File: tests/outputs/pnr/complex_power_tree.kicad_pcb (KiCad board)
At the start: 6 copper layers, 50 x 50 mm, 30 parts

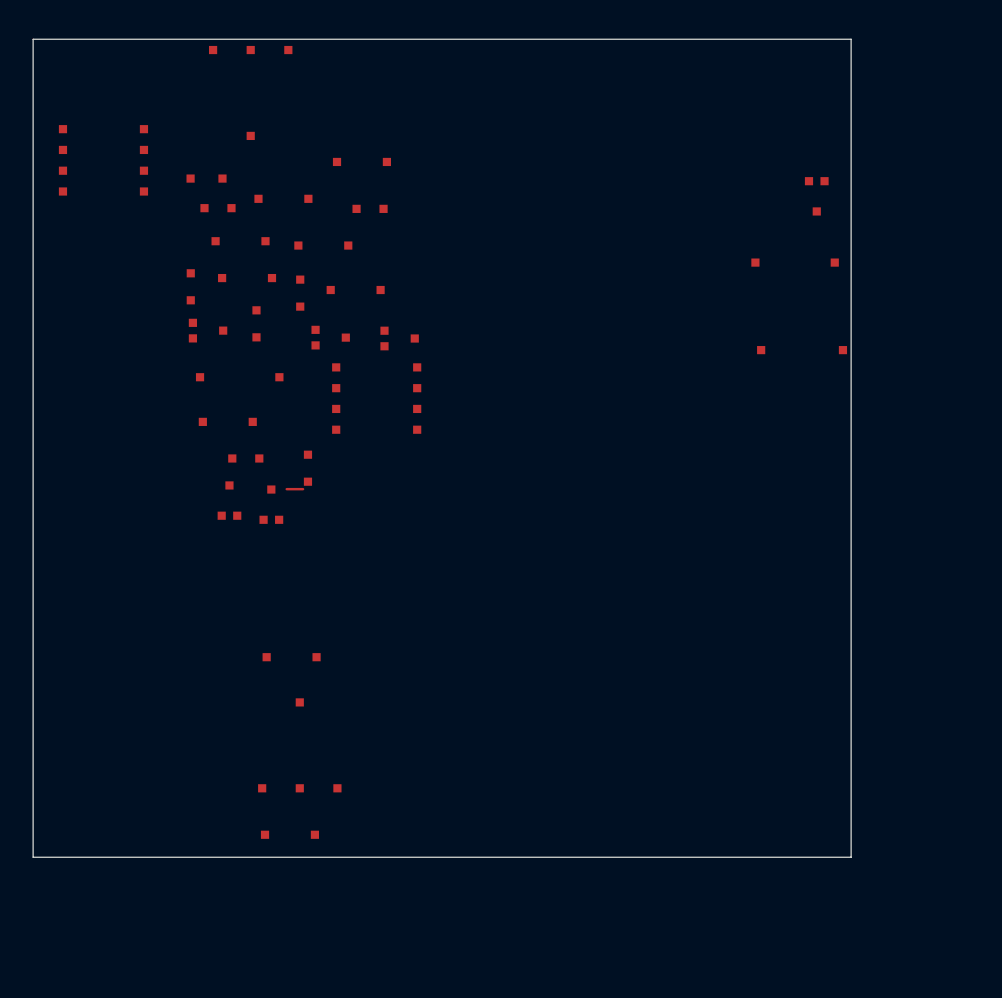
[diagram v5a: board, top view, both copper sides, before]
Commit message: feat: hierarchical block placement — zero overlaps
FPGA-inspired hierarchical placement:
1. Form blocks from functional groups + standalone components
2. Layout within blocks: IC center, caps flanking, inductors above,
   resistors below, diodes next to inductors
3. Place blocks on board using shelf packing (seed varies order)
4. Stamp block positions to individual components

Blocks guarantee zero overlaps since each block is pre-sized to
contain its children with internal routing margin.

Also: route through footprints — only block pad areas (not entire
component body), so traces can pass between pads.

Results on complex_power_tree.bhdl:
- Overlaps: 0 (was 2-19)
- 30/30 inside board
- Groups naturally clustered within blocks
- 16 blocks from 30 components (4 expansion + 12 singleton)
- Routability: 21% (routing channels now open between pads)

Co-Authored-By: Claude Opus 4.6 (1M context) <noreply@anthropic.com>
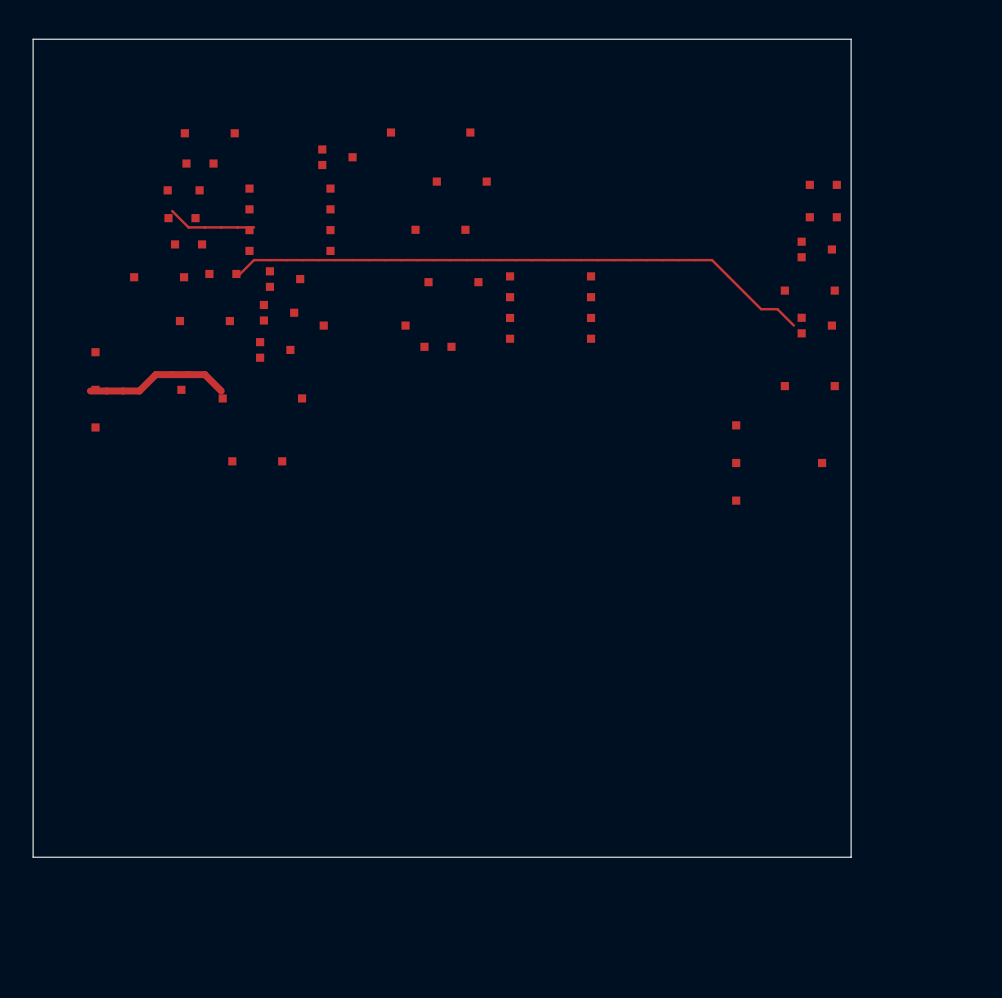
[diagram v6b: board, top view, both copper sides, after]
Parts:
- moved C5 42.0 mm to (47.5, 21.2)
- moved C4 38.8 mm to (47.5, 15.4), turned to 0 degrees
- moved R3 35.3 mm to (48.3, 10.9), turned to 0 degrees
- moved D4 35.1 mm to (47.9, 17.5), turned to 0 degrees
- moved U1 34.0 mm to (45.6, 25.9), turned to 360 degrees
- moved D2 33.6 mm to (15.0, 16.7), turned to 360 degrees
- moved R6 33.6 mm to (14.0, 22.0)
- moved R4 32.7 mm to (48.3, 8.90), turned to 360 degrees
- moved R2 26.8 mm to (20.3, 17.5)
- moved D3 26.1 mm to (47.9, 12.8)
- moved U2 19.4 mm to (6.44, 21.4), turned to 0 degrees
- moved C2 19.0 mm to (24.3, 5.70)
- moved R7 18.2 mm to (10.2, 7.60), turned to 360 degrees
- moved C9 13.7 mm to (10.5, 17.2), turned to 360 degrees
- moved R5 13.0 mm to (11.6, 14.3), turned to 0 degrees
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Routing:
- net 0: track 1.00 -> 50.3 mm

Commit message: feat: netlist-driven internal block layout
Replace template-based block layout with netlist-driven placement:
- For each child, find which IC pin it connects to via shared nets
- Place child on the side of IC where that pin is (left/right/top/bottom)
- Orient child so its connecting pin faces the IC
- Stack multiple children on the same side with spacing

Skip GND pins for side determination (GND connects everywhere).
Prefer signal/power pins that indicate actual signal flow direction.

3mm routing channels between blocks on the board.

Results: 6 overlaps (internal block stacking needs refinement),
29% routability with pad-only grid blockage.

Co-Authored-By: Claude Opus 4.6 (1M context) <noreply@anthropic.com>
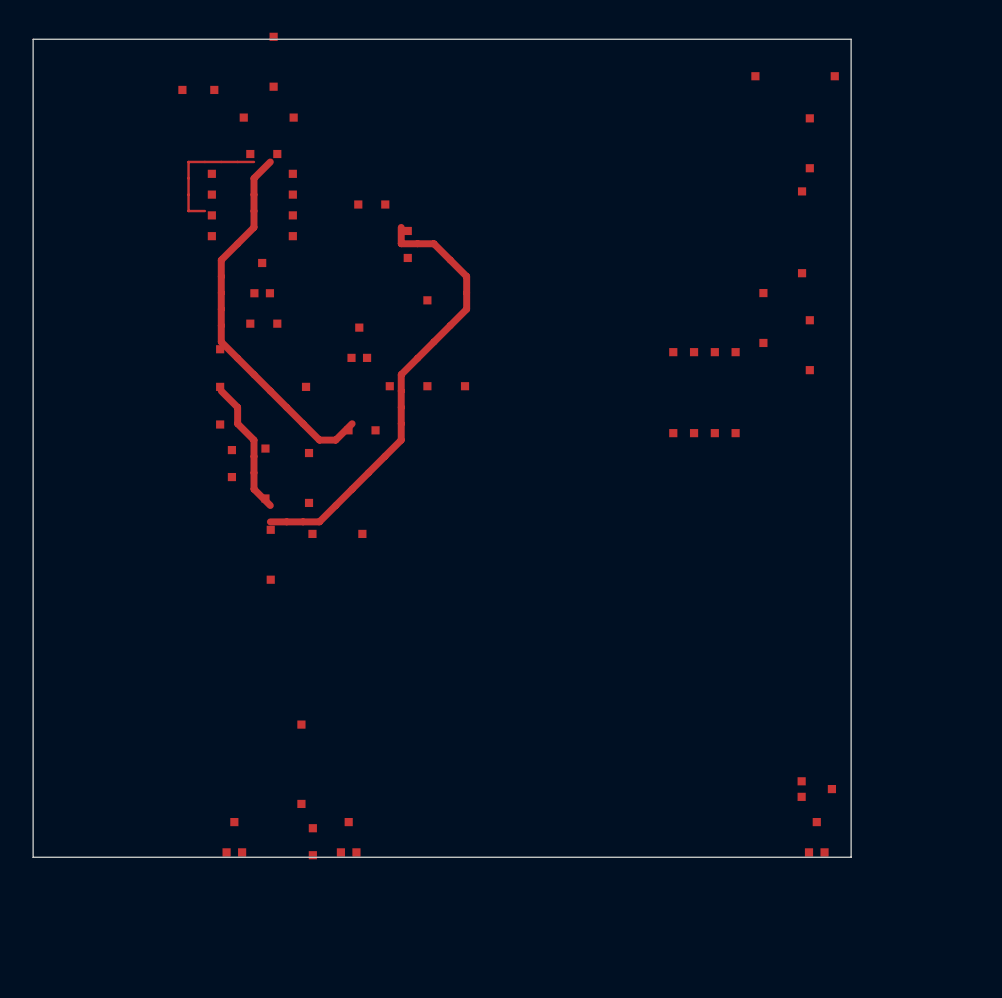
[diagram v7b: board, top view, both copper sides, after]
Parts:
- moved D3 50.6 mm to (12.3, 48.8), turned to 90 degrees
- moved D5 44.5 mm to (47.9, 48.8), turned to 90 degrees
- moved R7 42.0 mm to (17.1, 49.0), turned to 90 degrees
- moved R3 39.2 mm to (12.2, 25.9), turned to 90 degrees
- moved C4 36.7 mm to (14.5, 31.5), turned to 90 degrees
- moved D2 32.3 mm to (19.3, 48.8), turned to 90 degrees
- moved C5 30.3 mm to (18.6, 30.2)
- moved D4 28.3 mm to (47.9, 45.8)
- moved R4 27.6 mm to (20.7, 10.1)
- moved R2 27.3 mm to (47.0, 11.8), turned to 90 degrees
- moved U1 22.7 mm to (24.1, 18.6), turned to 90 degrees
- moved C2 22.5 mm to (46.6, 2.26)
- moved R6 22.5 mm to (16.4, 44.3), turned to 90 degrees
- moved L1 22.1 mm to (47.5, 18.7), turned to 90 degrees
- moved C8 21.9 mm to (16.9, 26.8), turned to 90 degrees
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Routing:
- net 0: track 50.3 -> 66.9 mm

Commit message: feat: placement { } language construct for datasheet-driven PCB layout
Add new BHDL language construct `placement { }` inside entity definitions
for encoding vendor-recommended component positions from IC datasheets.

Syntax:
    placement {
        reference "AP63205 Datasheet Fig.5";
        L_out at (0.0, -6.0) rot 0;
        C_out at (6.0, 0.0) rot 90;
        C_in  at (-6.0, 0.0) rot 90;
        C_bst at (3.5, -4.5) rot 0;
    }

Implementation across 7 crates:
- Parser: PLACEMENT_BLOCK/ITEM/REFERENCE syntax tokens, parse_placement_block()
- AST: PlacementBlock, PlacementItem node types with coordinate extraction
- Common: PlacementRecipe, ChildPosition data structures
- Analyzer: extract_placement_recipes() in Pass 8.5, imported file support
- PnR: blocks.rs matches recipes to expansion blocks, applies exact positions
- Stdlib: AP63205 entity now has placement block from datasheet Fig.5
- CLI: passes placement recipes from analyzer to PnR board

Data flow: stdlib placement {} → parser → AST → analyzer → PlacementRecipe
→ AnalysisResult → Board.placement_recipes → blocks.rs exact positioning

Test: AP63205 buck converter children placed at exact datasheet coordinates.
All 4 expansion blocks detected and using datasheet layout.
Routability: 21% → 43% (datasheet positions create better routing channels).

Co-Authored-By: Claude Opus 4.6 (1M context) <noreply@anthropic.com>
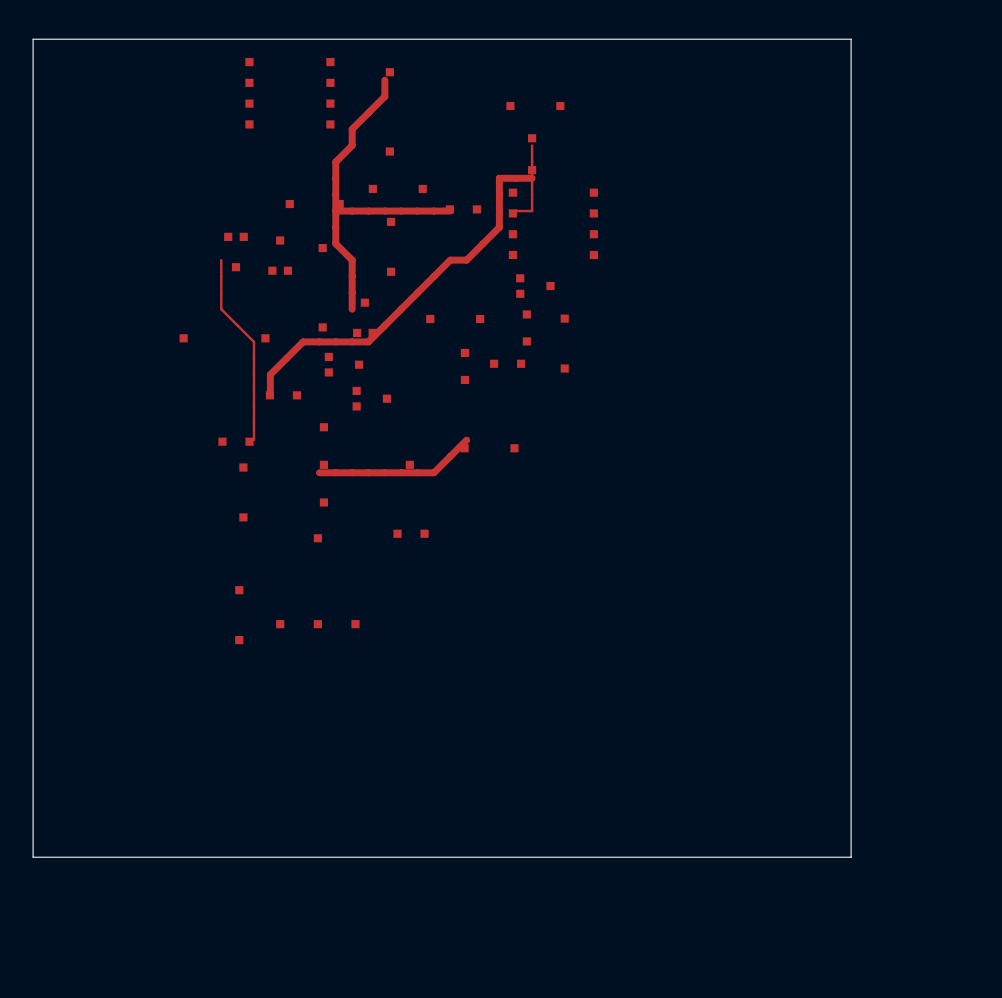
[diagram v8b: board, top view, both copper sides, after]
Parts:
- moved D5 50.4 mm to (12.4, 13.0), turned to 270 degrees
- moved D4 46.3 mm to (15.1, 13.2), turned to 90 degrees
- moved R2 35.9 mm to (11.7, 18.3), turned to 0 degrees
- moved X1 31.3 mm to (15.7, 3.30), turned to 0 degrees
- moved D3 29.6 mm to (19.0, 19.9), turned to 0 degrees
- moved R6 29.2 mm to (17.7, 15.2), turned to 270 degrees
- moved C1 28.3 mm to (17.2, 10.1), turned to 180 degrees
- moved D2 26.8 mm to (20.7, 22.0), turned to 360 degrees
- moved L1 26.3 mm to (21.9, 12.7)
- moved C3 25.3 mm to (22.3, 9.15), turned to 360 degrees
- moved R7 24.9 mm to (12.4, 24.6), turned to 360 degrees
- moved C2 24.9 mm to (21.8, 4.44), turned to 90 degrees
- moved C7 22.8 mm to (32.5, 18.6), turned to 270 degrees
- moved L2 20.8 mm to (30.5, 7.03), turned to 90 degrees
- moved R4 20.3 mm to (23.1, 30.2)
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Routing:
- net 0: track 66.9 -> 73.0 mm
